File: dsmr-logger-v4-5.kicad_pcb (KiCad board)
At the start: 2 copper layers, 66 x 50.8 mm, 43 parts, among them J1 RJ12 female connector (6P6C), J2 Jack-DC, J3 DC-or-SM-power, J4 I2C conn, J5 Programmer, J6 Test 3v3, J7 Test 5volt, J9 ADC 0-5v, Q1 BC547, SW1 RESET, SW2 FLASH, U1 LM2937xMP, U2 4N35, U3 ESP-12E

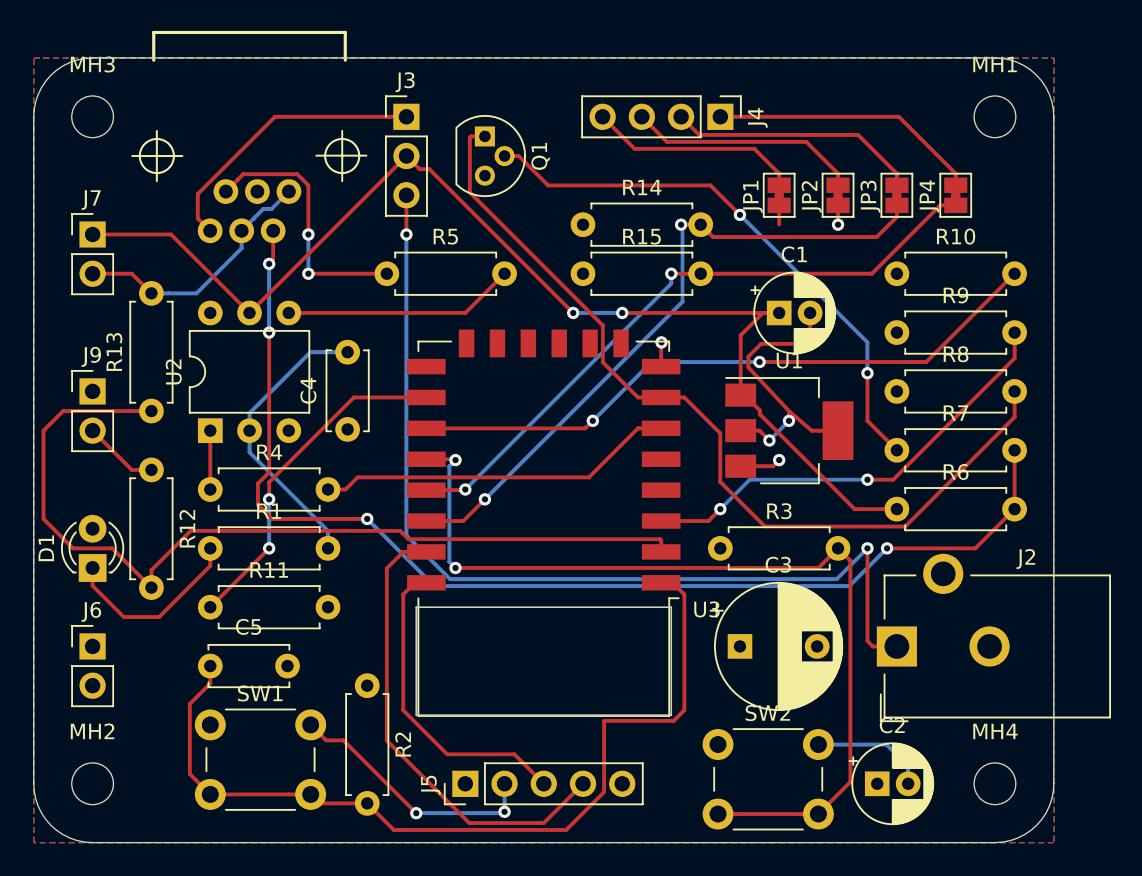
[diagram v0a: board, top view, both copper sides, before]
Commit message: Silk mask updated, changed JP4, added 3D renders
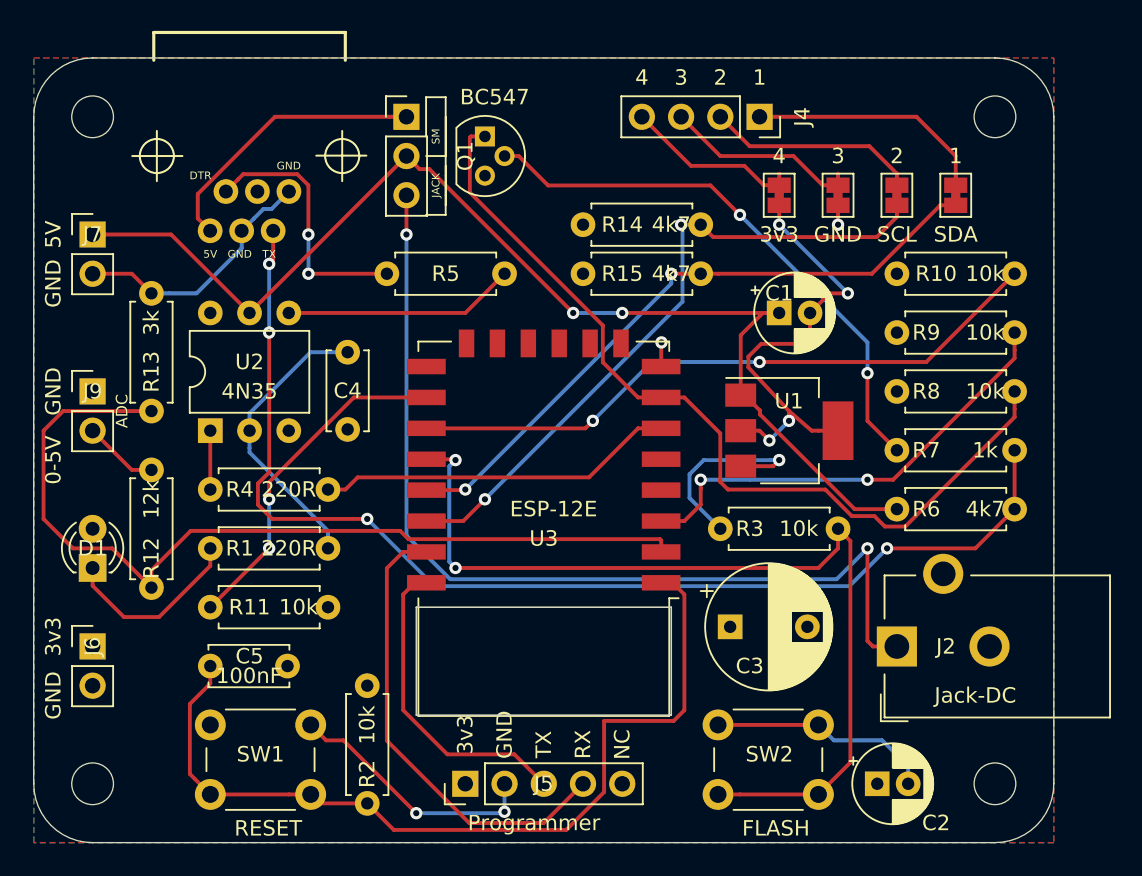
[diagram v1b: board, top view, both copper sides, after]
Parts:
- J4: footprint Connector_PinHeader_2.54mm:PinHeader_1x04_P2.54mm_Vertical -> Connector_PinSocket_2.54mm:PinSocket_1x04_P2.54mm_Vertical
- JP1: value Jumper_3v3 -> 3v3
- JP2: value Jumper_GND -> GND
- JP3: value Jumper_SCL -> SCL
- JP4: value Jumper_SDA -> SDA
- R12: value 12k (E24) -> 12k
- R13: value 3k (E24) -> 3k
- moved J4 2.54 mm to (157.5, 76.2)
- moved C3 1.42 mm to (155.6, 109.2)
- moved SW2 1.27 mm to (154.8, 115.6)
- moved R3 1.27 mm to (154.9, 102.9)
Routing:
- net GND: track 79.7 -> 96.9 mm, vias 4 -> 6
- net 3v3: track 5.48 -> 16.0 mm
- net Net-(J4-Pad2): track 16.2 -> 13.7 mm
- net Net-(J4-Pad4): track 13.7 -> 11.5 mm
- net Net-(J4-Pad3): track 15.0 -> 12.7 mm
- net GPIO0: track 59.4 -> 60.7 mm
- net Net-(J4-Pad1): track 17.5 -> 16.4 mm
- net Net-(R9-Pad2): track 28.9 -> 29.9 mm
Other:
- board text added: "0-5V"
- board text added: "1"
- board text added: "2"
- board text added: "3"
- board text added: "3v3"
- board text added: "4"
- board text added: "5V"
- board text added: "ADC"
- board text added: "DTR"
- board text added: "GND"
- board text added: "JACK"
- board text added: "NC"
- board text added: "RX"
- board text added: "SM"
- board text added: "TX"
